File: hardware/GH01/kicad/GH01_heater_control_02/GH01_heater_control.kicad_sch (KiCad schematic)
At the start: 9 parts

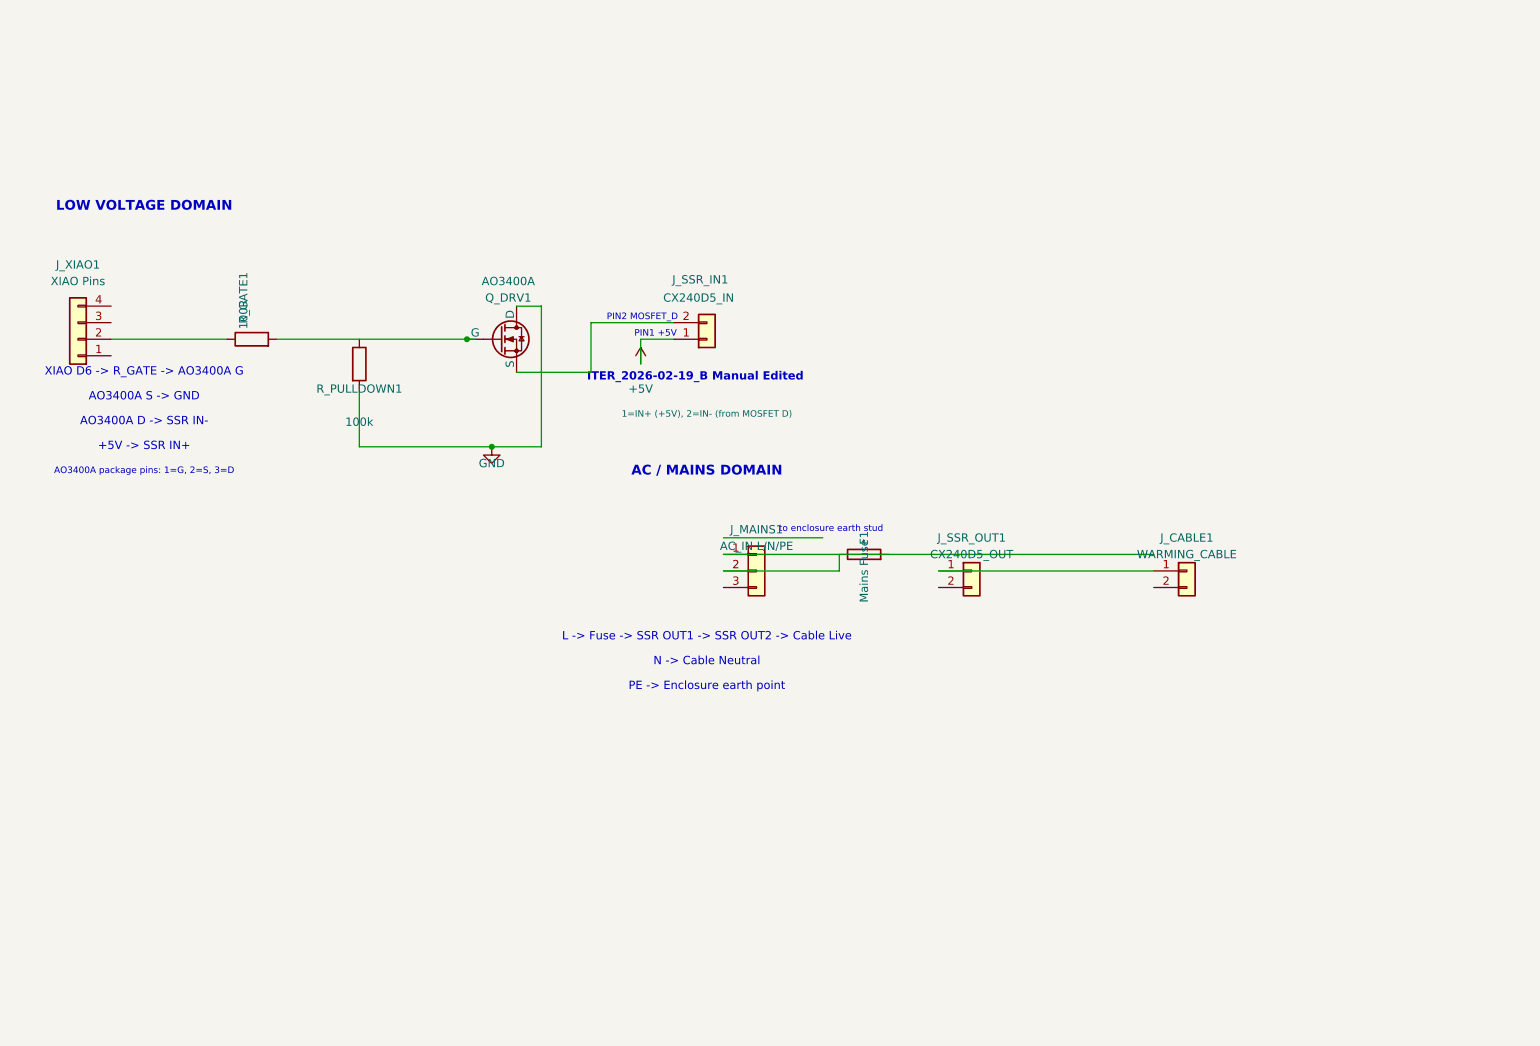
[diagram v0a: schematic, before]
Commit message: hardware/gh01: finalize V2 schematic baseline with clean ERC and matrix
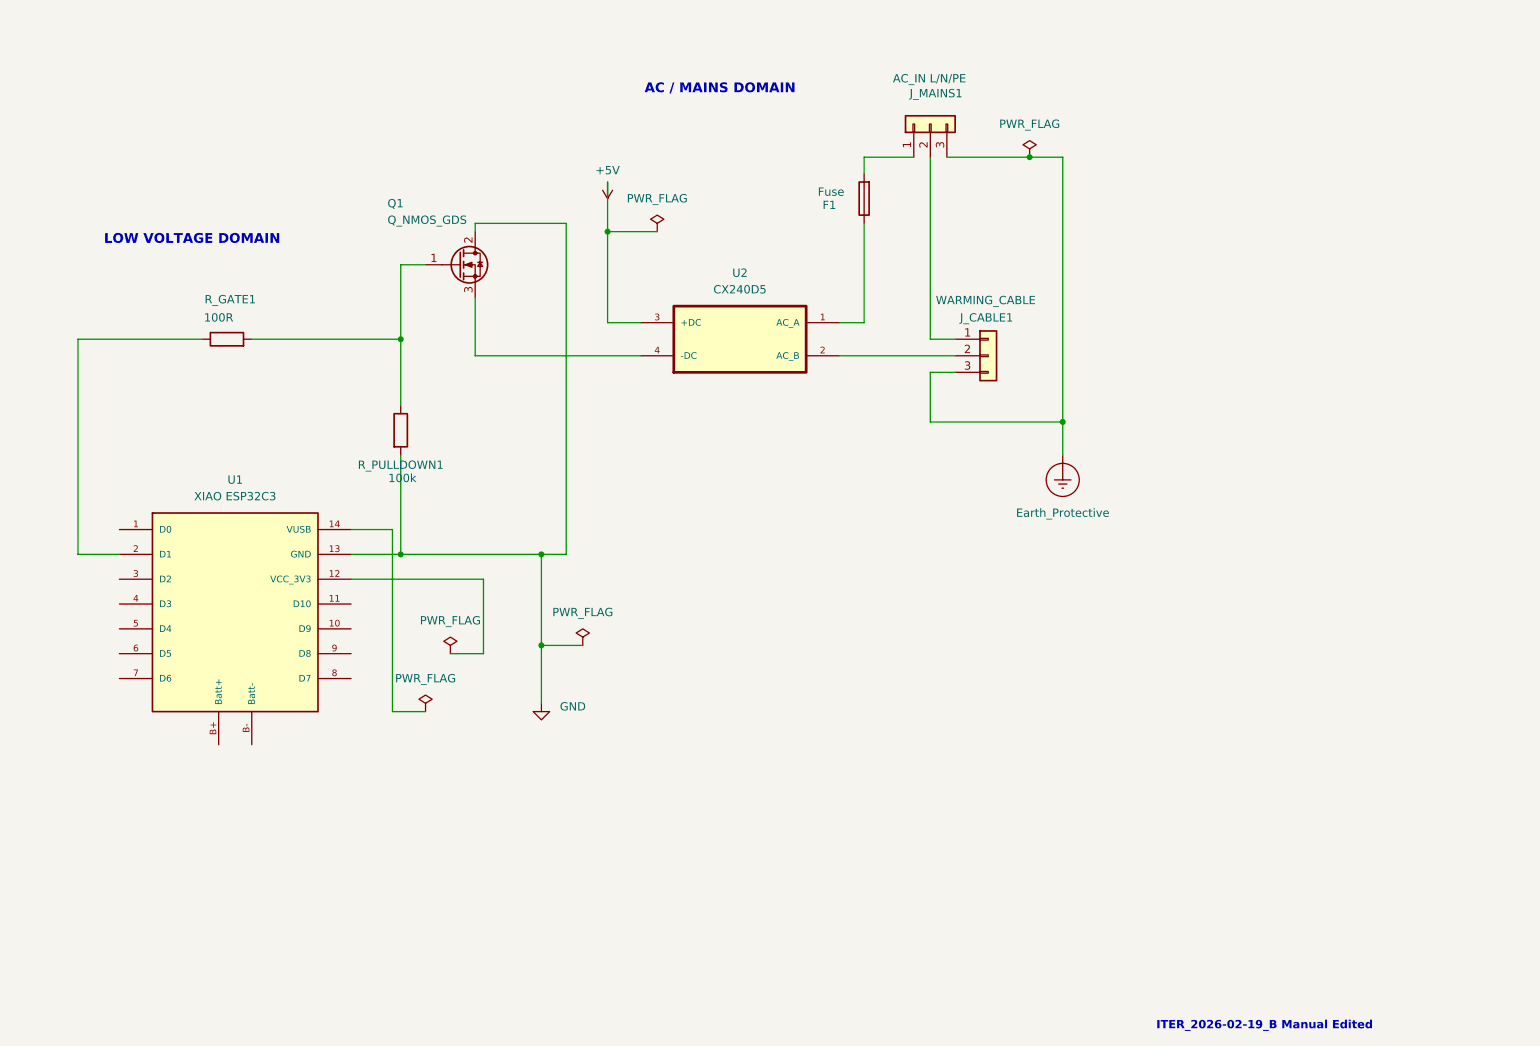
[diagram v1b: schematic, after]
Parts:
- removed J_CABLE1: WARMING_CABLE, symbol Connector_Generic:Conn_01x02
- removed J_SSR_IN1: CX240D5_IN, symbol Connector_Generic:Conn_01x02
- removed J_SSR_OUT1: CX240D5_OUT, symbol Connector_Generic:Conn_01x02
- removed J_XIAO1: XIAO Pins, symbol Connector_Generic:Conn_01x04
- removed Q_DRV1: AO3400A, Package_TO_SOT_SMD:SOT-23, symbol Device:Q_NMOS_GDS
- added J_CABLE1: WARMING_CABLE, symbol Connector_Generic:Conn_01x03
- added Q1: Q_NMOS_GDS, symbol Transistor_FET:Q_NMOS_GDS
- added U1: XIAO ESP32C3, XIAO_ESP32C3:ESP32-C3, symbol xiao_esp32c3:XIAO ESP32C3
- added U2: CX240D5, CX240D5:CRYDOM_CX240D5, symbol CX240D5:CX240D5
- F1: value Mains Fuse -> Fuse
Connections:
- net +5V: now also U2.3 (+DC)
- net GND: now also Q1.2 (D), U1.13 (GND)
- net at R_GATE1.1: now also U1.2 (D1)
- net at R_GATE1.2: now also R_PULLDOWN1.1, Q1.1 (G)
- net at J_MAINS1.1 (Pin_1): now also F1.2
- net at F1.1: now also U2.1 (AC_A); no longer J_MAINS1.2 (Pin_2)
- net Earth_Protective: now reaches J_MAINS1.3 (Pin_3)
- net Earth_Protective: now also J_CABLE1.3 (Pin_3)
- new net: J_CABLE1.2 (Pin_2), U2.2 (AC_B)
- new net: Q1.3 (S), U2.4 (-DC)
- new net: J_CABLE1.1 (Pin_1), J_MAINS1.2 (Pin_2)
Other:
- note removed: "+5V -> SSR IN+"
- note removed: "AO3400A D -> SSR IN-"
- note removed: "AO3400A S -> GND"
- note removed: "AO3400A package pins: 1=G, 2=S, 3=D"
- note removed: "L -> Fuse -> SSR OUT1 -> SSR OUT2 -> Cable Live"
- note removed: "N -> Cable Neutral"
- note removed: "PE -> Enclosure earth point"
- note removed: "PIN1 +5V"
- note removed: "PIN2 MOSFET_D"
- note removed: "XIAO D6 -> R_GATE -> AO3400A G"
- note removed: "to enclosure earth stud"
- moved on the sheet: J_MAINS1, R_GATE1, R_PULLDOWN1

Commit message: hardware/gh01: add AZ-Delivery PSU symbol and schematic updates
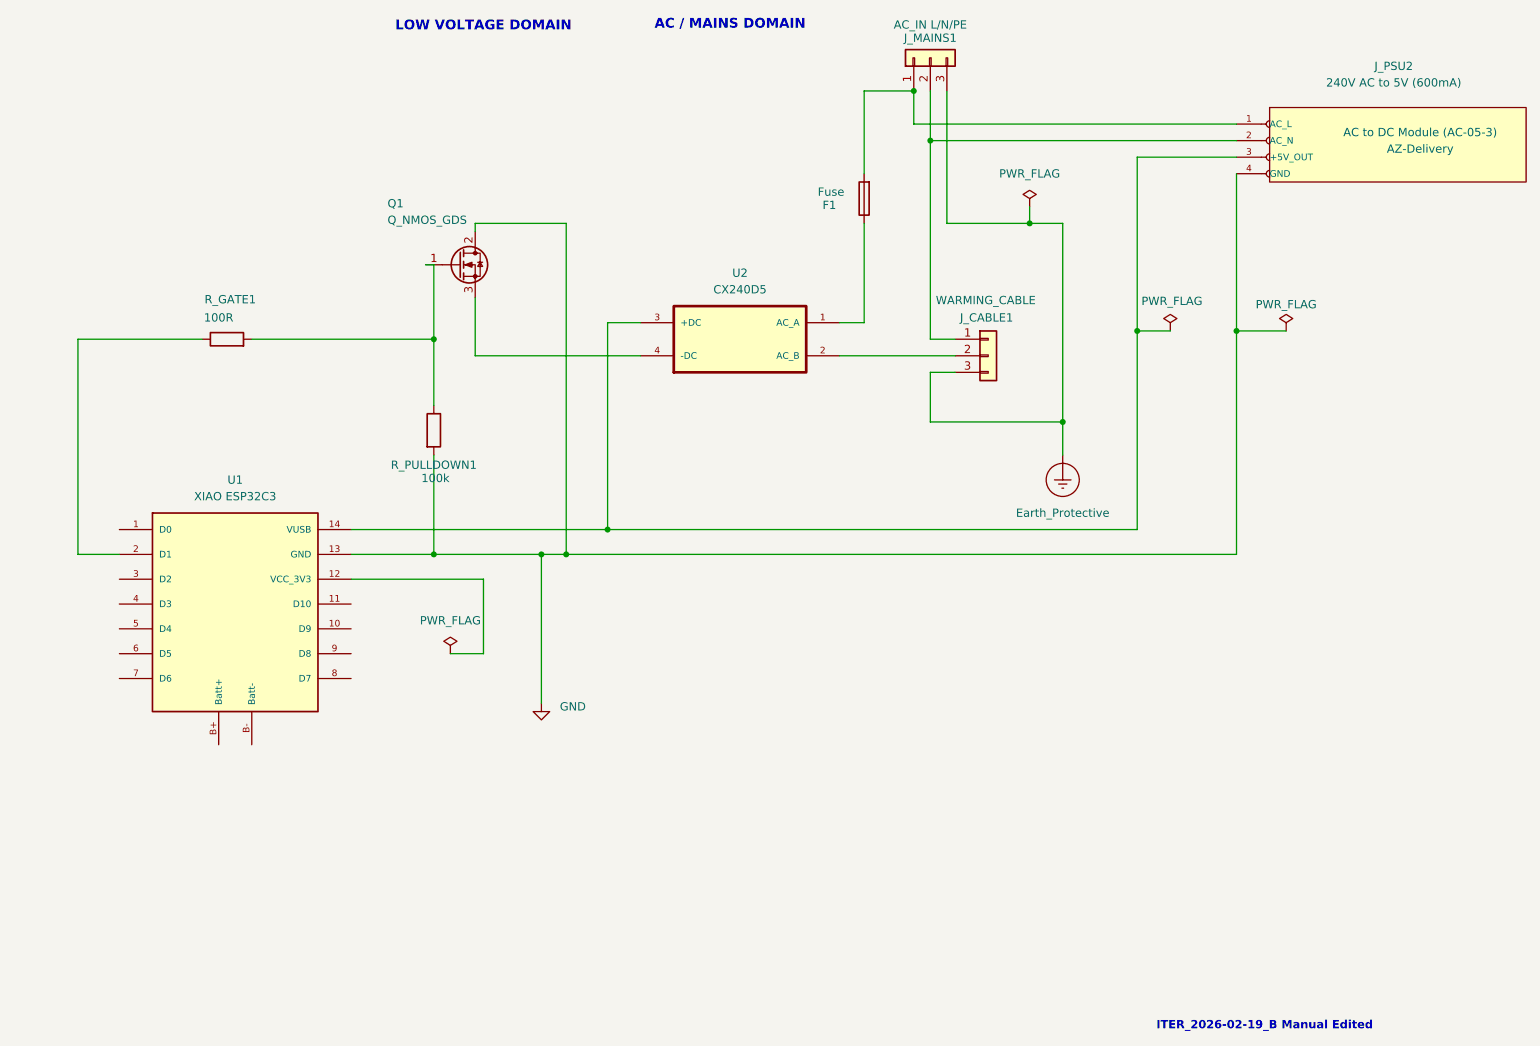
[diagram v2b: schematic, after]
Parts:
- added J_PSU2: 240V AC to 5V (600mA), symbol AZ_Delivery:AC_to_5V_DC_Module
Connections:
- net +5V is gone; now on an unnamed net: U2.3 (+DC)
- net GND: now also J_PSU2.4 (GND)
- net at F1.2, J_MAINS1.1 (Pin_1): now also J_PSU2.1 (AC_L)
- net at J_CABLE1.1 (Pin_1), J_MAINS1.2 (Pin_2): now also J_PSU2.2 (AC_N)
- net at U1.14 (VUSB): now also J_PSU2.3 (+5V_OUT)
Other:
- moved on the sheet: J_MAINS1, R_PULLDOWN1

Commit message: GH01 V2 design updates
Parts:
- removed F1: Fuse, symbol Device:Fuse
- removed Q1: Q_NMOS_GDS, symbol Transistor_FET:Q_NMOS_GDS
- added D1: 1N5819, Diode_THT:D_DO-41_SOD81_P10.16mm_Horizontal, symbol Diode:1N5819
- added F2: Fuse, symbol Device:Fuse
- added Q1: BS170, Package_TO_SOT_THT:TO-92_Inline, symbol Transistor_FET:BS170
- renumbered U2 to SSR1
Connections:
- net GND: now also Q1.3 (S)
- net at SSR1.1 (AC_A): now also J_PSU2.1 (AC_L), F2.1
- net at J_MAINS1.1 (Pin_1): now also F2.2; no longer J_PSU2.1 (AC_L)
- net at SSR1.2 (AC_B): now also J_CABLE1.1 (L); no longer J_CABLE1.2 (Pin_2)
- net at SSR1.3 (+DC), U1.14 (VUSB): now also D1.1 (K); no longer J_PSU2.3 (+5V_OUT)
- net at SSR1.4 (-DC): now also Q1.1 (D)
- net at J_MAINS1.2 (Pin_2), J_PSU2.2 (AC_N): now also J_CABLE1.2 (N); no longer J_CABLE1.1 (Pin_1)
- net at R_GATE1.2, R_PULLDOWN1.1: now also Q1.2 (G)
- new net: D1.2 (A), J_PSU2.3 (+5V_OUT)
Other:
- moved on the sheet: J_MAINS1, J_PSU2, R_GATE1, R_PULLDOWN1, SSR1, U1
